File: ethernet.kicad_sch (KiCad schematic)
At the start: 40 parts, among them J1001 7499010121A, U1001 LAN8742A-CZ-TR, U1002 USBLC6-4SC6

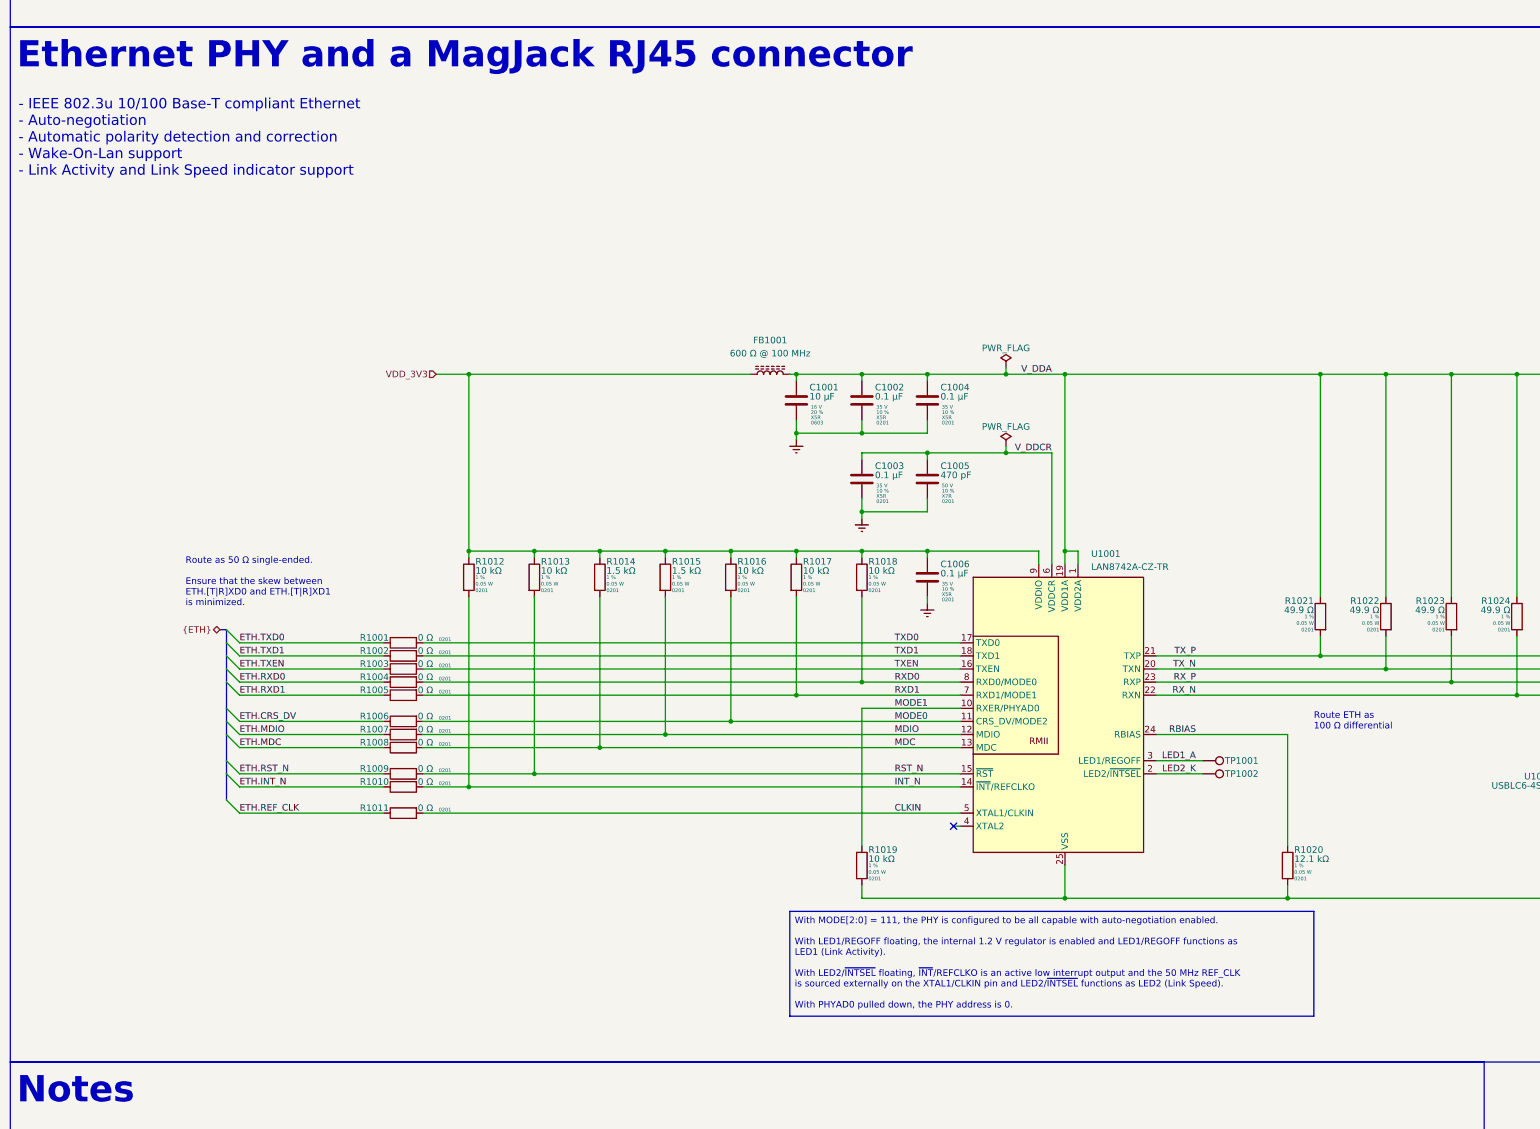
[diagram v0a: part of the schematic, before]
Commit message: Refactor text with ChatGPT and make schematics more readable
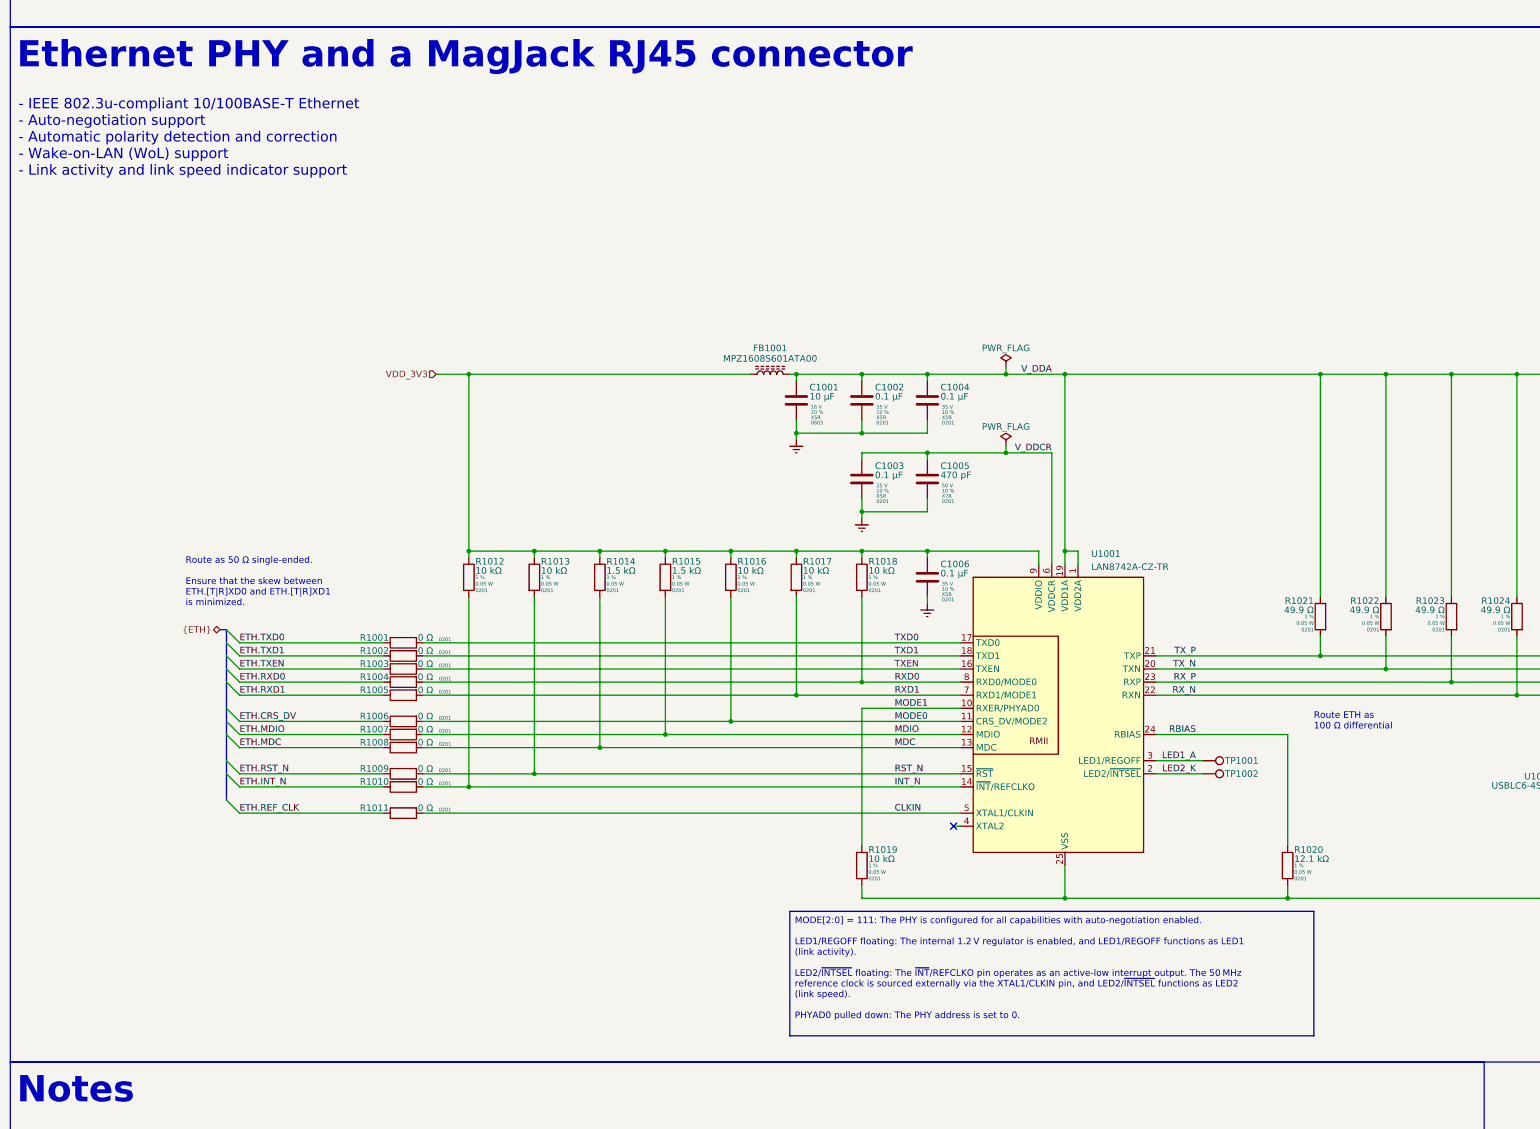
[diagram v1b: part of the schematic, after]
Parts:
- FB1001: value 600 Ω @ 100 MHz -> MPZ1608S601ATA00
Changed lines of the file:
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@@
 		)
 	)
-	(text_box "With MODE[2:0] = 111, the PHY is configured to be all capable with auto-negotiation enabled.\n\nWith LED1/REGOFF floating, the internal 1.2 V regulator is enabled and LED1/REGOFF functions as LED1 (Link Activity).\n\nWith LED2/~{INTSEL} floating, ~{INT}/REFCLKO is an active low interrupt output and the 50 MHz REF_CLK is sourced externally on the XTAL1/CLKIN pin and LED2/~{INTSEL} functions as LED2 (Link Speed).\n\nWith PHYAD0 pulled down, the PHY address is 0."
+	(text_box "MODE[2:0] = 111: The PHY is configured for all capabilities with auto-negotiation enabled.\n\nLED1/REGOFF floating: The internal 1.2 V regulator is enabled, and LED1/REGOFF functions as LED1 (link activity).\n\nLED2/~{INTSEL} floating: The ~{INT}/REFCLKO pin operates as an active-low interrupt output. The 50 MHz reference clock is sourced externally via the XTAL1/CLKIN pin, and LED2/~{INTSEL} functions as LED2 (link speed).\n\nPHYAD0 pulled down: The PHY address is set to 0."
 		(exclude_from_sim no)
 		(at 163.83 222.25 0)
-		(size 101.6 20.32)
+		(size 101.6 24.13)
 		(margins 0.9525 0.9525 0.9525 0.9525)
 		(stroke
@@
 		)
 	)
-	(text_box "- IEEE 802.3u 10/100 Base-T compliant Ethernet\n- Auto-negotiation\n- Automatic polarity detection and correction\n- Wake-On-Lan support\n- Link Activity and Link Speed indicator support"
+	(text_box "- IEEE 802.3u-compliant 10/100BASE-T Ethernet\n- Auto-negotiation support\n- Automatic polarity detection and correction\n- Wake-on-LAN (WoL) support\n- Link activity and link speed indicator support"
 		(exclude_from_sim no)
 		(at 13.335 63.5 0)
@@
 		(dnp no)
 		(property "Reference" "FB1001"
-			(at 160.02 112.268 90)
+			(at 160.02 113.792 90)
 			(effects
 				(font
@@
 			)
 		)
-		(property "Value" "600 Ω @ 100 MHz"
-			(at 160.02 114.808 90)
+		(property "Value" "MPZ1608S601ATA00"
+			(at 160.02 115.824 90)
 			(effects
 				(font
@@
 			)
 		)
-		(property "Datasheet" "~"
+		(property "Datasheet" "https://product.tdk.com/en/system/files?file=dam/doc/product/emc/emc/beads/catalog/beads_commercial_power_mpz1608_en.pdf"
 			(at 160.02 118.11 0)
 			(effects
@@
 			)
 		)
-		(property "Description" "Inductor with ferrite core"
+		(property "Description" "600 Ohms @ 100 MHz 1 Power Line Ferrite Bead 0603 (1608 Metric) 1A 150mOhm"
 			(at 160.02 118.11 0)
 			(effects

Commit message: Rework ethernet
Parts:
- FB1001: value MPZ1608S601ATA00 -> BLM18PG121SN1D; Digi-Key Part Number 445-MPZ1608S601ATA00CT-ND -> 490-1037-1-ND; MPN MPZ1608S601ATA00 -> BLM18PG121SN1D; Manufacturer TDK Corporation -> Murata Electronics
- renumbered C1003 to C1002, C1006 to C1003, C1005 to C1004, C1004 to C1005, C1002 to C1006
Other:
- moved on the sheet: C1001, C1002, C1004, C1005, C1006, FB1001

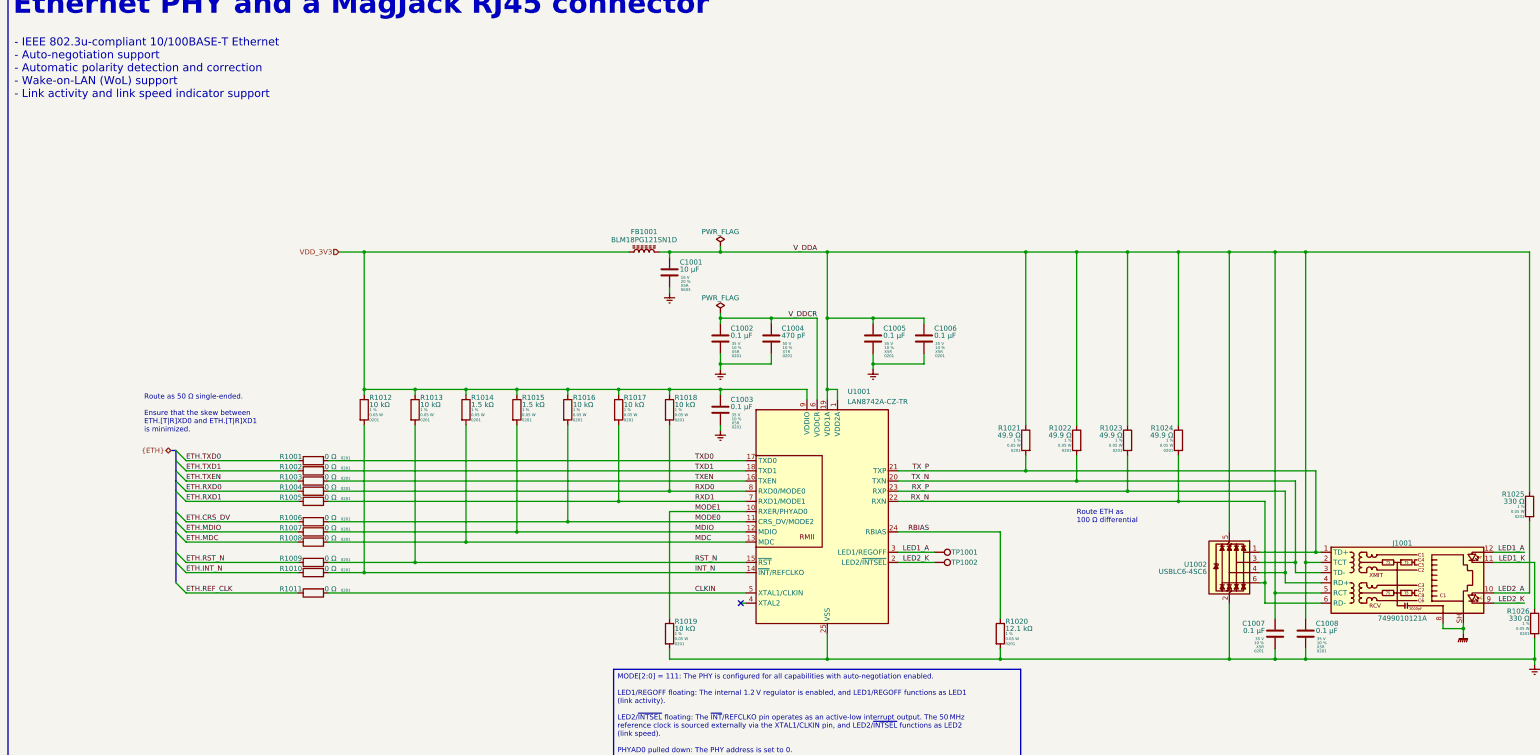
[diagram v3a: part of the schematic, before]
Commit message: Ethernet: Fix TVS
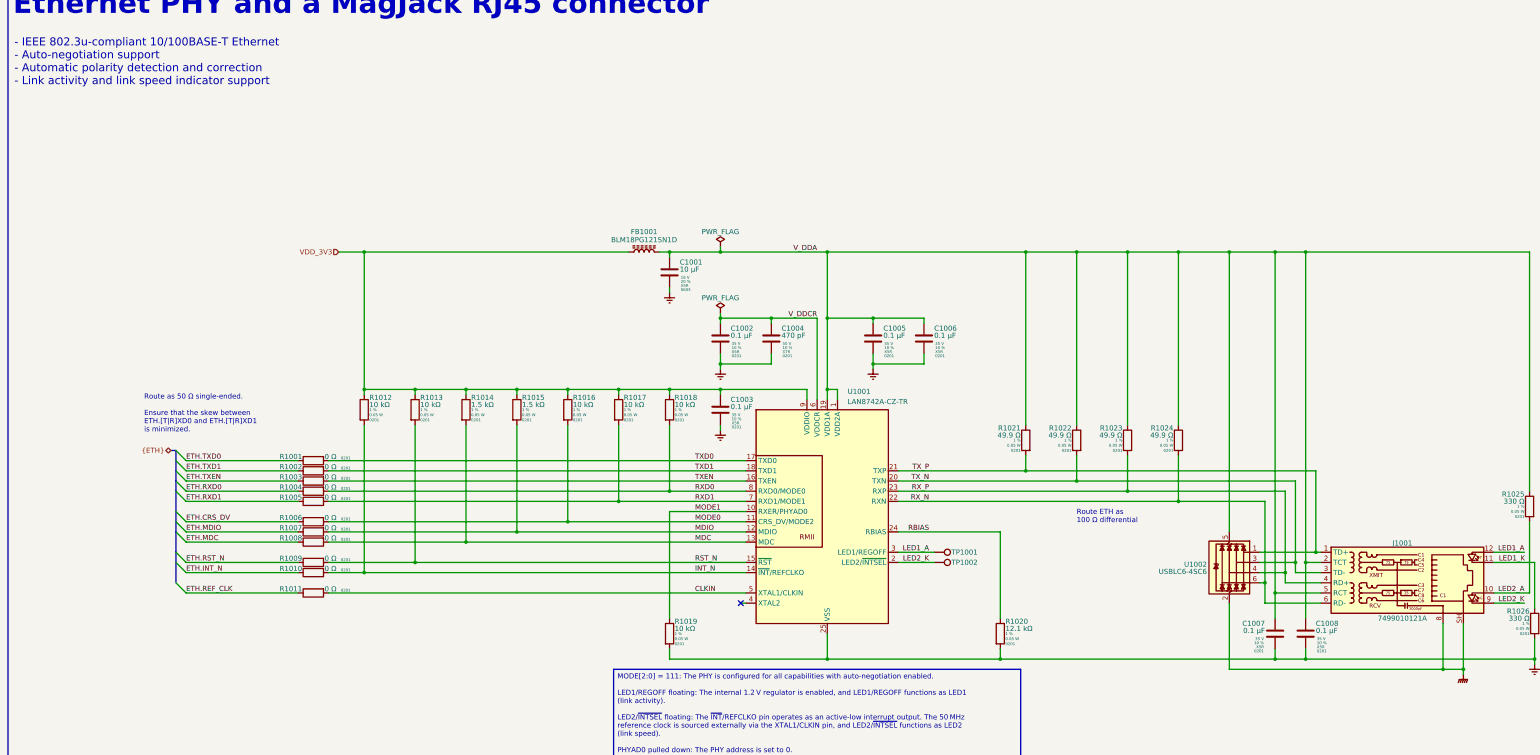
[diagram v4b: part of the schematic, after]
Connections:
- net CHASSIS: now also U1002.2 (GND)
- net GND: no longer U1002.2 (GND)
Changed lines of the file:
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@@
 		)
 	)
-	(text_box "- IEEE 802.3u-compliant 10/100BASE-T Ethernet\n- Auto-negotiation support\n- Automatic polarity detection and correction\n- Wake-on-LAN (WoL) support\n- Link activity and link speed indicator support"
+	(text_box "- IEEE 802.3u-compliant 10/100BASE-T Ethernet\n- Auto-negotiation support\n- Automatic polarity detection and correction\n- Link activity and link speed indicator support"
 		(exclude_from_sim no)
 		(at 13.335 63.5 0)
@@
 	)
 	(junction
+		(at 375.92 222.25)
+		(diameter 0)
+		(color 0 0 0 0)
+	)
+	(junction
 		(at 217.17 219.71)
 		(diameter 0)
@@
 	)
 	(junction
+		(at 370.84 222.25)
+		(diameter 0)
+		(color 0 0 0 0)
+	)
+	(junction
 		(at 114.3 152.4)
 		(diameter 0)
@@
 	)
 	(junction
-		(at 317.5 219.71)
-		(diameter 0)
-		(color 0 0 0 0)
-	)
-	(junction
 		(at 217.17 152.4)
 		(diameter 0)
@@
 	)
 	(junction
-		(at 375.92 212.09)
-		(diameter 0)
-		(color 0 0 0 0)
-	)
-	(junction
 		(at 228.6 134.62)
 		(diameter 0)
@@
 	(wire
 		(pts
-			(xy 260.35 219.71) (xy 317.5 219.71)
+			(xy 260.35 219.71) (xy 328.93 219.71)
 		)
 		(stroke
@@
 	(wire
 		(pts
-			(xy 317.5 219.71) (xy 328.93 219.71)
-		)
-		(stroke
-			(width 0)
-			(type default)
-		)
-	)
-	(wire
-		(pts
 			(xy 228.6 134.62) (xy 228.6 135.89)
 		)
@@
 	(wire
 		(pts
-			(xy 370.84 212.09) (xy 375.92 212.09)
-		)
-		(stroke
-			(width 0)
-			(type default)
-		)
-	)
-	(wire
-		(pts
 			(xy 139.7 152.4) (xy 139.7 153.67)
 		)
@@
 	(wire
 		(pts
+			(xy 370.84 222.25) (xy 375.92 222.25)
+		)
+		(stroke
+			(width 0)
+			(type default)
+		)
+	)
+	(wire
+		(pts
 			(xy 234.95 193.04) (xy 243.84 193.04)
 		)
@@
 	(wire
 		(pts
-			(xy 375.92 210.82) (xy 375.92 212.09)
+			(xy 375.92 210.82) (xy 375.92 222.25)
 		)
 		(stroke
@@
 	(wire
 		(pts
-			(xy 375.92 213.36) (xy 375.92 212.09)
+			(xy 375.92 223.52) (xy 375.92 222.25)
 		)
 		(stroke
@@
 	(wire
 		(pts
+			(xy 317.5 222.25) (xy 370.84 222.25)
+		)
+		(stroke
+			(width 0)
+			(type default)
+		)
+	)
+	(wire
+		(pts
 			(xy 217.17 219.71) (xy 217.17 213.36)
 		)
@@
 	(wire
 		(pts
+			(xy 317.5 205.74) (xy 317.5 222.25)
+		)
+		(stroke
+			(width 0)
+			(type default)
+		)
+	)
+	(wire
+		(pts
 			(xy 304.8 118.11) (xy 304.8 161.29)
 		)
@@
 	(wire
 		(pts
-			(xy 370.84 210.82) (xy 370.84 212.09)
+			(xy 370.84 210.82) (xy 370.84 222.25)
 		)
 		(stroke
@@
 	(wire
 		(pts
-			(xy 317.5 205.74) (xy 317.5 219.71)
-		)
-		(stroke
-			(width 0)
-			(type default)
-		)
-	)
-	(wire
-		(pts
 			(xy 234.95 195.58) (xy 243.84 195.58)
 		)
@@
 	(symbol
 		(lib_id "power:GNDPWR")
-		(at 375.92 213.36 0)
+		(at 375.92 223.52 0)
 		(unit 1)
 		(exclude_from_sim no)
@@
 		(fields_autoplaced yes)
 		(property "Reference" "#PWR01005"
-			(at 375.92 218.44 0)
+			(at 375.92 228.6 0)
 			(effects
 				(font
@@
 		)
 		(property "Value" "CHASSIS"
-			(at 375.793 217.17 0)
+			(at 375.793 227.33 0)
 			(effects
 				(font
@@
 		)
 		(property "Footprint" ""
-			(at 375.92 214.63 0)
+			(at 375.92 224.79 0)
 			(effects
 				(font
@@
 		)
 		(property "Datasheet" ""
-			(at 375.92 214.63 0)
+			(at 375.92 224.79 0)
 			(effects
 				(font
@@
 		)
 		(property "Description" "Power symbol creates a global label with name \"GNDPWR\" , global ground"
-			(at 375.92 213.36 0)
+			(at 375.92 223.52 0)
 			(effects
 				(font

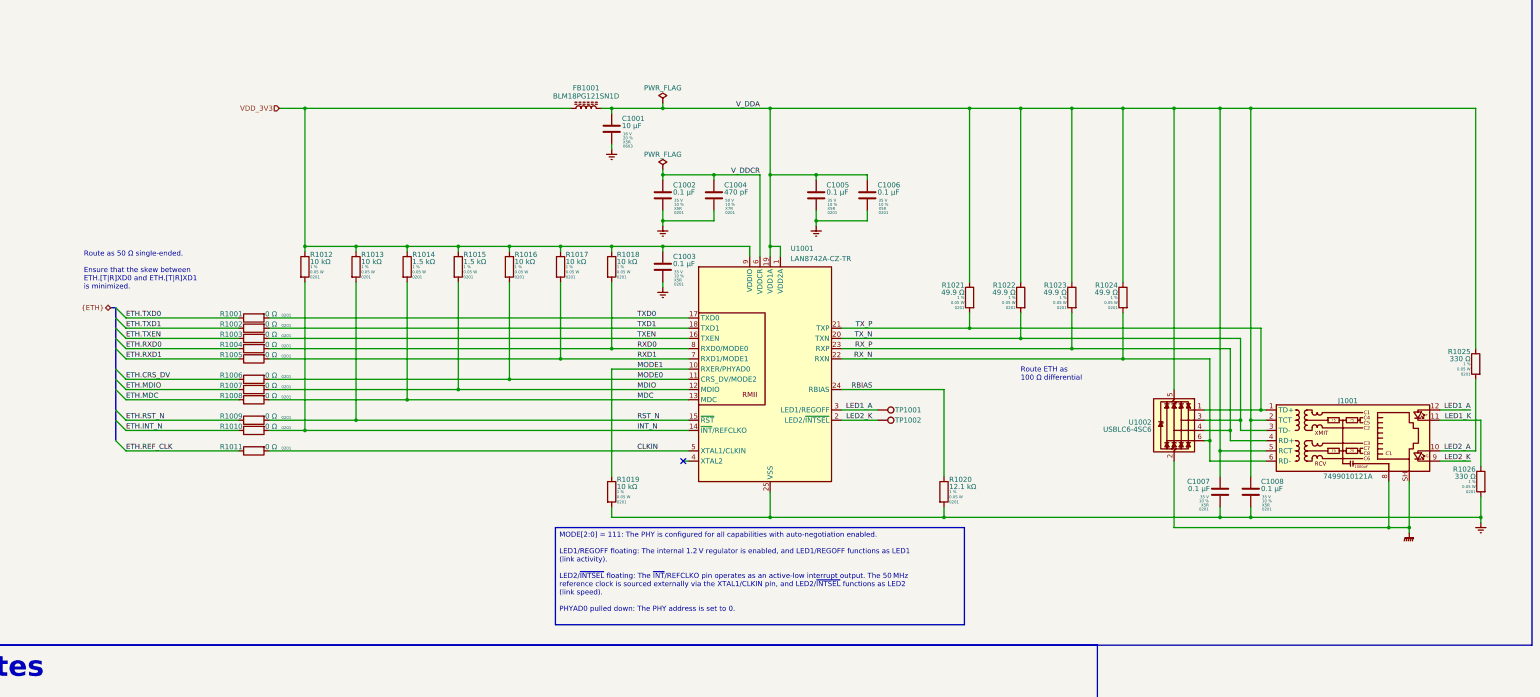
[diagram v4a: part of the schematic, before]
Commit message: Fix power connections
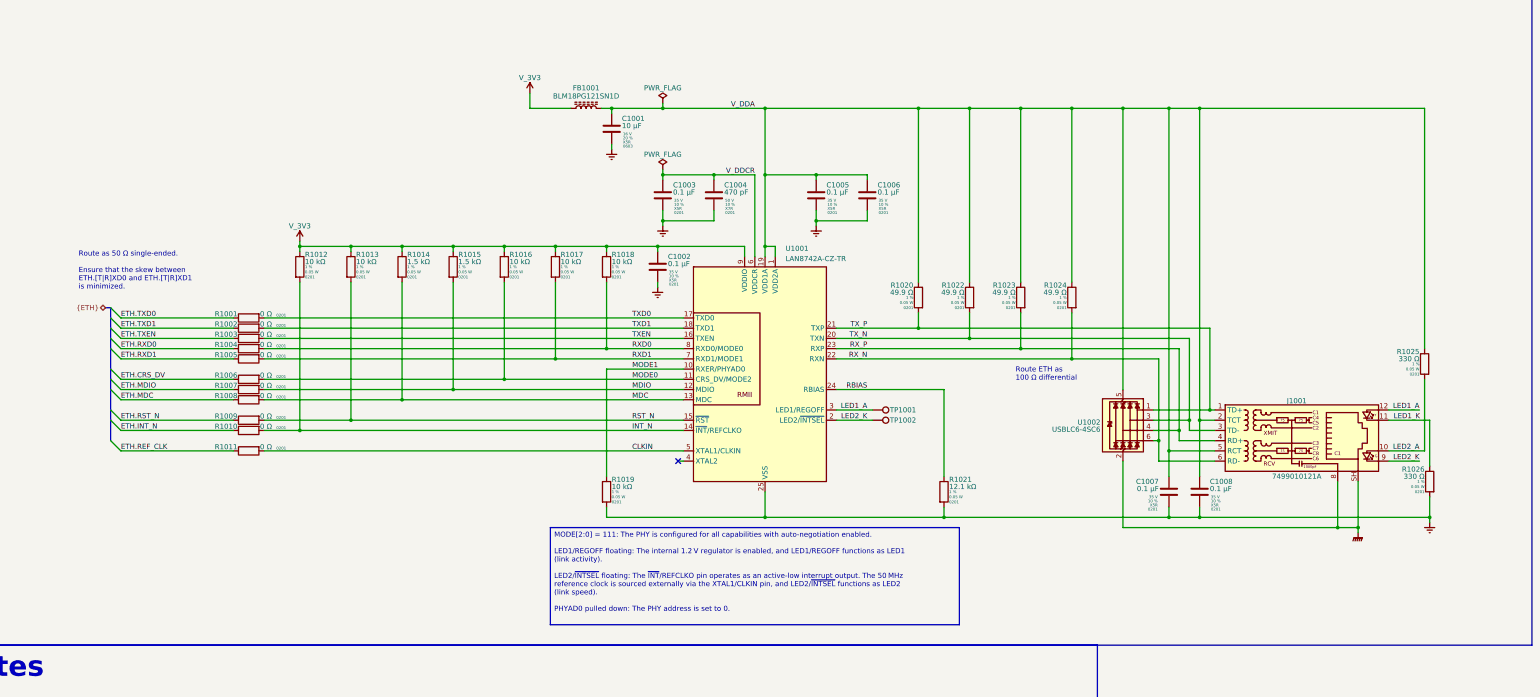
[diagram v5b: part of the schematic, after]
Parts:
- renumbered C1003 to C1002, C1002 to C1003, R1021 to R1020, R1020 to R1021
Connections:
- net VDD_3V3 renamed V_3V3
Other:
- moved on the sheet: C1002, C1007, C1008, J1001, R1001, R1002, R1003, R1004, R1005, R1006, R1007, R1008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
